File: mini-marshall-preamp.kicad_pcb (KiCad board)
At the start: 2 copper layers, 133.4 x 76.5 mm, 46 parts, among them J1 LO, J2 HI, J3 OUT, J4 6V3, J5 370V GND, J6 370V, J7 6V3 GND, J8 6V3, J9 6V3 GND, U1 6N2P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

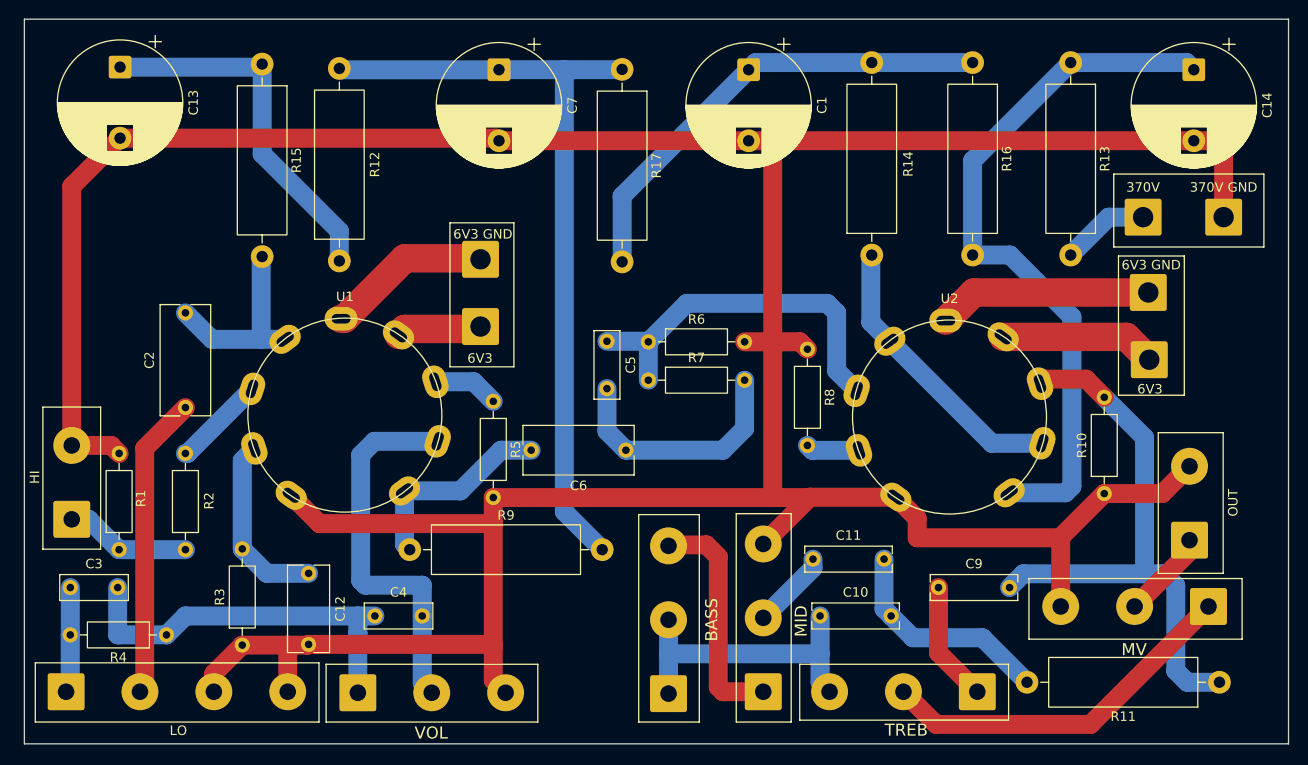
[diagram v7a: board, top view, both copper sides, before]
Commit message: Add mounting holes
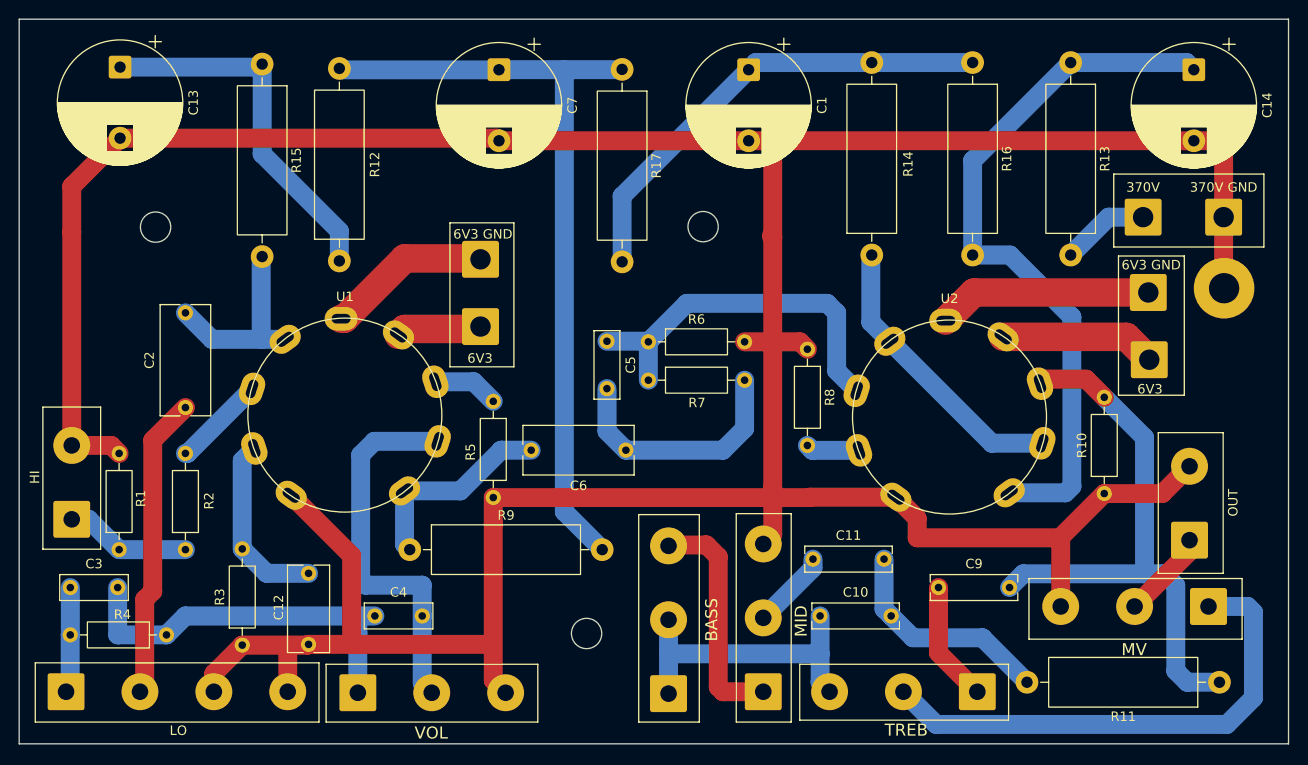
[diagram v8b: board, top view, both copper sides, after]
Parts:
- added H3: MountingHole_Pad, MountingHole:MountingHole_3.2mm_M3_Pad, F.Cu at (179.7, 78.4)
- added H4: MountingHole_Pad, MountingHole:MountingHole_3.2mm_M3, F.Cu at (124.7, 71.9)
- added H5: MountingHole_Pad, MountingHole:MountingHole_3.2mm_M3, F.Cu at (112.3, 114.8)
- added H6: MountingHole_Pad, MountingHole:MountingHole_3.2mm_M3, F.Cu at (66.8, 72.0)
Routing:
- net Net-(RV2-Pad2): track 38.8 -> 53.6 mm
- net GND: track 384.2 -> 386.8 mm
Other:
- board size 133.4 x 76.5 mm -> 134 x 76.5 mm
